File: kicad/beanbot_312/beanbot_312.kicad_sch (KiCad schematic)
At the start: 66 parts, among them M1 P&O2_VOEDING, M10 P&O2_MEETPUNT, M11 P&O2_ULTRASONE_HC_SR04, M12 P&O2_MEETPUNT, M13 P&O2_MEETPUNT, M14 P&O2_GEWICHTSENSOR, M15 P&O2_MEETPUNT, M16 P&O2_MEETPUNT, M17 P&O2_MEETPUNT, M18 P&O2_MEETPUNT, M19 P&O2_MEETPUNT, M2 P&O2_MEETPUNT, M20 P&O2_KLEURSENSOR, M21 P&O2_MEETPUNT, M22 P&O2_MEETPUNT, M23 P&O2_RESISTOR, M24 P&O2_MEETPUNT, M25 P&O2_RESISTOR, M26 P&O2_RESISTOR, M27 P&O2_MEETPUNT, M28 P&O2_DC-MOTOR, M29 P&O2_RESISTOR, M3 P&O2_RESISTOR, M30 P&O2_MEETPUNT, M31 P&O2_DC-MOTOR, M32 P&O2_MEETPUNT, M33 P&O2_RESISTOR, M34 P&O2_MEETPUNT, M35 P&O2_RESISTOR, M36 P&O2_RESISTOR, M37 P&O2_MEETPUNT, M38 P&O2_DC-MOTOR, M39 P&O2_RESISTOR, M4 P&O2_MEETPUNT, M40 P&O2_MEETPUNT, M41 P&O2_DC-MOTOR, M42 P&O2_MEETPUNT, M43 P&O2_RESISTOR, M44 P&O2_MEETPUNT, M45 P&O2_RESISTOR, M46 P&O2_RESISTOR, M47 P&O2_MEETPUNT, M48 P&O2_DC-MOTOR, M49 P&O2_RESISTOR, M5 P&O2_RGB_LED, M50 P&O2_MEETPUNT, M51 P&O2_DC-MOTOR, M52 P&O2_MEETPUNT, M53 P&O2_MOSFET, M54 P&O2_MOSFET, M55 P&O2_MOSFET, M56 P&O2_MOSFET, M57 P&O2_MOSFET, M58 P&O2_MOSFET, M6 P&O2_RESISTOR, M7 P&O2_MEETPUNT, M8 P&O2_RESISTOR, M9 P&O2_RESISTOR, U1 P&O2_ARDUINO_MEGA, U2 LCD-016N002L

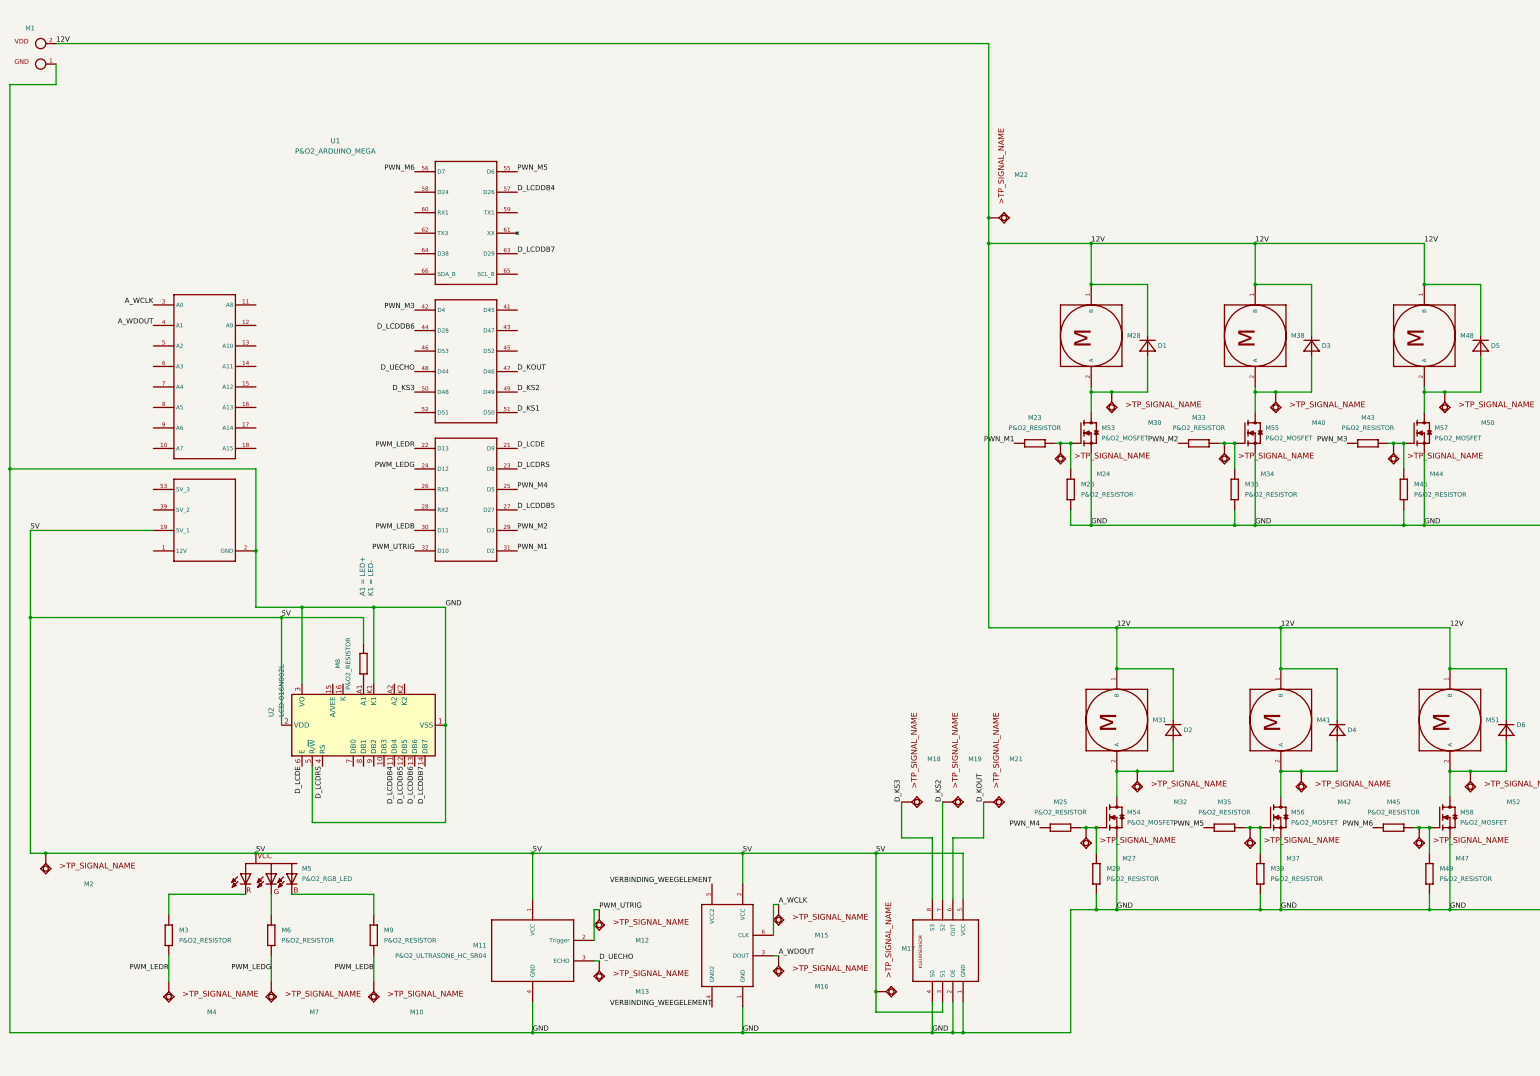
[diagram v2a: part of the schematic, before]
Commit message: Add KiCad changes (#13)
* Added IC to KiCad

* Latest changes

* Fixed scheme

* Changed DC to servomotor

* Latest changes

* Refactored schematic

Co-authored-by: Robin Martens <robin.martens@quivr.be>
Co-authored-by: Rob Nickmans <rob.nickmans@rndevelopment.be>
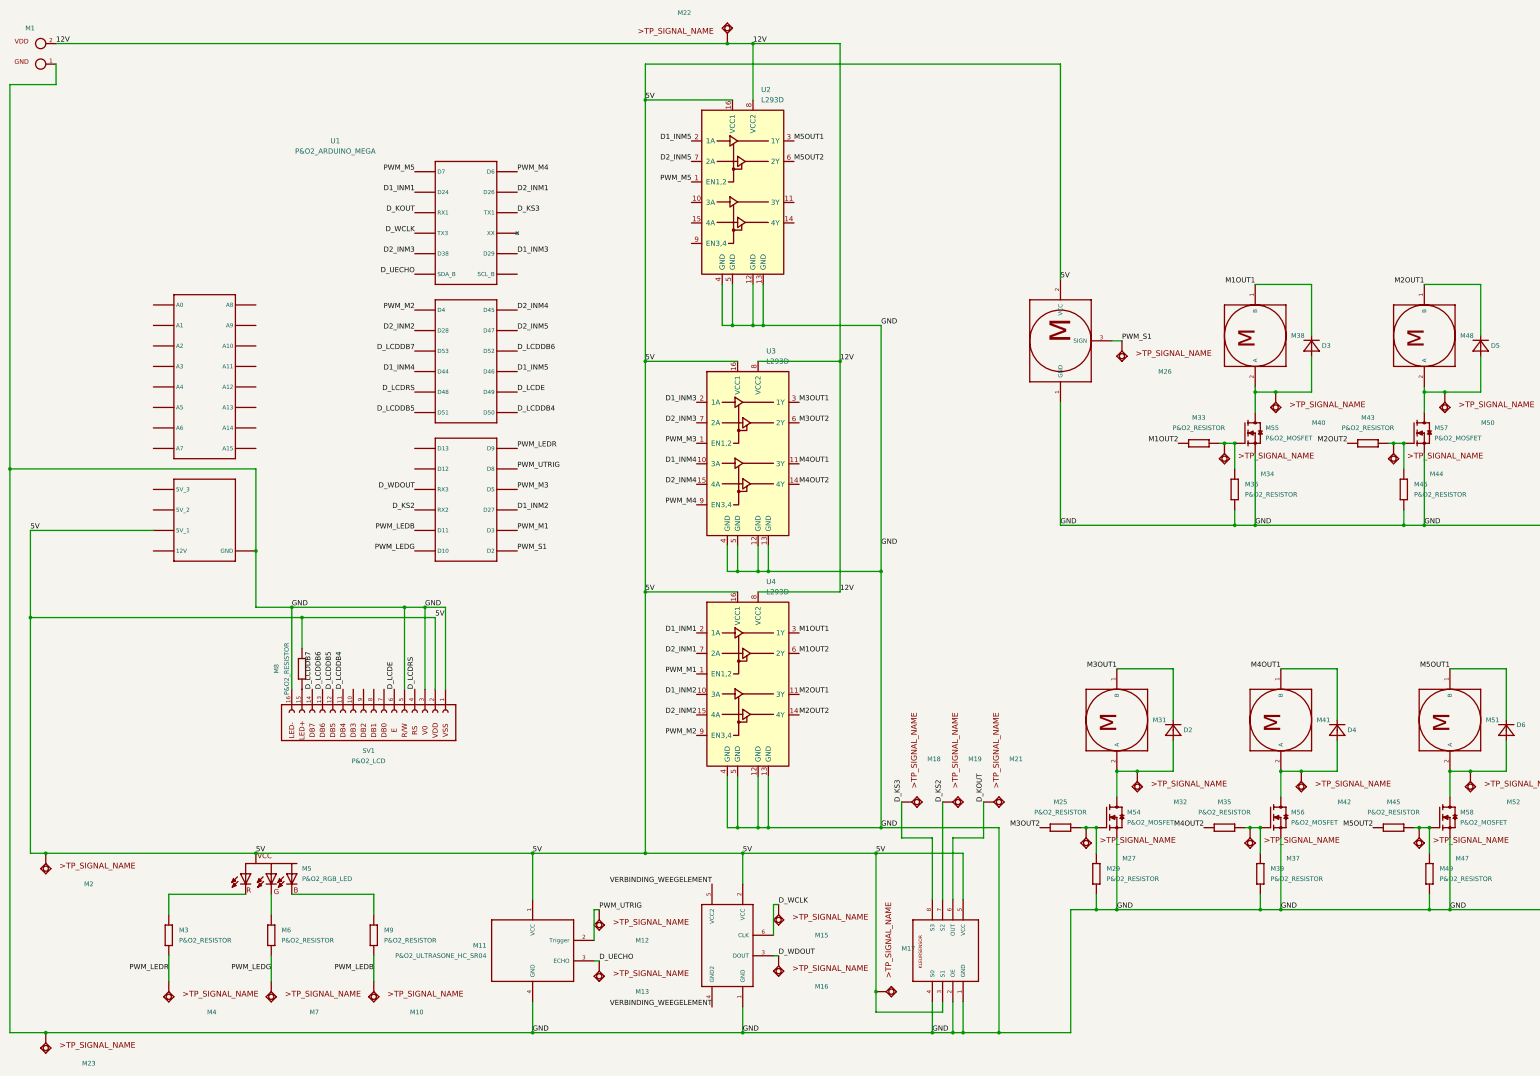
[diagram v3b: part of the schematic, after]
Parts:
- removed D1: P&O2_DIODE, 1_P&O2_lib:P&O2_DIODE, symbol 1_P&O2_lib:P&O2_DIODE
- removed M23, M26: P&O2_RESISTOR, 1_P&O2_lib:P&O2_RES, symbol 1_P&O2_lib:P&O2_RESISTOR
- removed M24, M30: P&O2_MEETPUNT, 1_P&O2_lib:P&O2_MEETPUNT, symbol 1_P&O2_lib:P&O2_MEETPUNT
- removed M28: P&O2_DC-MOTOR, 1_P&O2_lib:P&O2_2PIN-SCREW-5.08, symbol 1_P&O2_lib:P&O2_DC-MOTOR
- removed M53: P&O2_MOSFET, 1_P&O2_lib:P&O2_TO220, symbol 1_P&O2_lib:P&O2_MOSFET
- removed U2: LCD-016N002L, Display:LCD-016N002L, symbol Display_Character:LCD-016N002L
- added M23, M26: P&O2_MEETPUNT, 1_P&O2_lib:P&O2_MEETPUNT, symbol 1_P&O2_lib:P&O2_MEETPUNT
- added M24: P&O2_SERVOMOTOR, P&O2_lib_SERVO-3PIN, symbol 1_P&O2_lib:P&O2_SERVOMOTOR
- added SV1: P&O2_LCD, P&O2_lib_FE05-1, symbol 1_P&O2_lib:P&O2_LCD
- added U2, U3, U4: L293D, Package_DIP:DIP-16_W7.62mm, symbol Driver_Motor:L293D
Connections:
- net D_KS1 is gone; now on net D_LCDDB4: U1.51 (D50)
- net 12V: now also U2.8 (VCC2), U3.8 (VCC2), U4.8 (VCC2); no longer D2.C, D3.C, D4.C, D5.C, D6.C, M31.1 (B), M38.1 (B), M41.1 (B), M48.1 (B), M51.1 (B)
- net 5V: now also M24.2 (VCC), SV1.2, U2.16 (VCC1), U3.16 (VCC1), U4.16 (VCC1)
- net D_KOUT: now also U1.60 (RX1); no longer U1.47 (D46)
- net D_KS2: now also U1.28 (RX2); no longer U1.49 (D49)
- net D_KS3: now also U1.59 (TX1); no longer U1.50 (D48)
- net D_LCDDB4: now also SV1.11; no longer U1.57 (D26)
- net D_LCDDB5: now also U1.52 (D51), SV1.12; no longer U1.27 (D27)
- net D_LCDDB6: now also U1.45 (D52), SV1.13; no longer U1.44 (D28)
- net D_LCDDB7: now also U1.46 (D53), SV1.14; no longer U1.63 (D29)
- net D_LCDE: now also U1.49 (D49), SV1.6; no longer U1.21 (D9)
- net D_LCDRS: now also U1.50 (D48), SV1.4; no longer U1.23 (D8)
- net D_UECHO: now also U1.66 (SDA_B); no longer U1.48 (D44)
- net GND: now also M23.1 (TP), M24.1 (GND), SV1.1, SV1.16, SV1.3, SV1.5, U2.12 (GND), U2.13 (GND), U2.4 (GND), U2.5 (GND), U3.12 (GND), U3.13 (GND), U3.4 (GND), U3.5 (GND), U4.12 (GND), U4.13 (GND), U4.4 (GND), U4.5 (GND)
- net PWM_LEDG: now also U1.32 (D10); no longer U1.24 (D12)
- net PWM_LEDR: now also U1.21 (D9); no longer U1.22 (D13)
- net PWM_UTRIG: now also U1.23 (D8); no longer U1.32 (D10)
- net at M8.1: now also SV1.15
- net D_WDOUT: now reaches U1.26 (RX3)
- net D_WDOUT: now also M14.3 (DOUT), M16.1 (TP)
- net D2_INM4: now reaches U1.41 (D45)
- net D2_INM4: now also U3.15 (4A)
- net D2_INM5: now reaches U1.43 (D47)
- net D2_INM5: now also U2.7 (2A)
- net D1_INM1: now reaches U1.58 (D24)
- net D1_INM1: now also U4.2 (1A)
- net D_WCLK: now reaches U1.62 (TX3)
- net D_WCLK: now also M14.6 (CLK), M15.1 (TP)
- net D2_INM3: now reaches U1.64 (D38)
- net D2_INM3: now also U3.7 (2A)
- removed net A_WCLK: M14.6 (CLK), M15.1 (TP), U1.3 (A0)
- removed net A_WDOUT: M14.3 (DOUT), M16.1 (TP), U1.4 (A1)
- net PWN_M1 renamed PWM_S1
- net PWM_S1: now also M24.3 (SIGN), M26.1 (TP)
- net PWN_M2 renamed M1OUT2
- net M1OUT2: now also U4.6 (2Y); no longer U1.29 (D3)
- net PWN_M3 renamed M2OUT2
- net M2OUT2: now also U4.14 (4Y); no longer U1.42 (D4)
- net PWN_M4 renamed M3OUT2
- net M3OUT2: now also U3.6 (2Y); no longer U1.25 (D5)
- net PWN_M5 renamed M4OUT2
- net M4OUT2: now also U3.14 (4Y); no longer U1.55 (D6)
- net PWN_M6 renamed M5OUT2
- net M5OUT2: now also U2.6 (2Y); no longer U1.56 (D7)
- new net D1_INM2: U1.27 (D27), U4.10 (3A)
- new net D1_INM3: U1.63 (D29), U3.2 (1A)
- new net D1_INM4: U1.48 (D44), U3.10 (3A)
- new net D1_INM5: U1.47 (D46), U2.2 (1A)
- new net D2_INM1: U1.57 (D26), U4.7 (2A)
- new net D2_INM2: U1.44 (D28), U4.15 (4A)
- new net M1OUT1: D3.C, M38.1 (B), U4.3 (1Y)
- new net M2OUT1: D5.C, M48.1 (B), U4.11 (3Y)
- new net M3OUT1: D2.C, M31.1 (B), U3.3 (1Y)
- new net M4OUT1: D4.C, M41.1 (B), U3.11 (3Y)
- new net M5OUT1: D6.C, M51.1 (B), U2.3 (1Y)
- new net PWM_M1: U1.29 (D3), U4.1 (EN1,2)
- new net PWM_M2: U1.42 (D4), U4.9 (EN3,4)
- new net PWM_M3: U1.25 (D5), U3.1 (EN1,2)
- new net PWM_M4: U1.55 (D6), U3.9 (EN3,4)
- new net PWM_M5: U1.56 (D7), U2.1 (EN1,2)
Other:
- note removed: "A1 = LED+ K1 = LED-"
- moved on the sheet: M22

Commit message: Kicad Redraw (#25)
* kicad redraw

* Added labels and measuring point

* Latest KiCad changes

* Restore latest version

Co-authored-by: Robin Martens <robin.martens@quivr.be>
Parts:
- removed D2, D3, D4, D5, D6: P&O2_DIODE, 1_P&O2_lib:P&O2_DIODE, symbol 1_P&O2_lib:P&O2_DIODE
- removed M1: P&O2_VOEDING, 1_P&O2_lib:P&O2_2PIN-SCREW-5.08, symbol 1_P&O2_lib:P&O2_VOEDING
- removed M10, M15, M16, M22, M23, M26, M32, M34, M37, M4, M44, M47, M7: P&O2_MEETPUNT, 1_P&O2_lib:P&O2_MEETPUNT, symbol 1_P&O2_lib:P&O2_MEETPUNT
- removed M14: P&O2_GEWICHTSENSOR, 1_P&O2_lib:P&O2_GEWICHTSENSOR-6PIN, symbol 1_P&O2_lib:P&O2_GEWICHTSENSOR
- removed M24: P&O2_SERVOMOTOR, P&O2_lib_SERVO-3PIN, symbol 1_P&O2_lib:P&O2_SERVOMOTOR
- removed M25, M29, M33, M35, M36, M39, M43, M49: P&O2_RESISTOR, 1_P&O2_lib:P&O2_RES, symbol 1_P&O2_lib:P&O2_RESISTOR
- removed M31, M38, M41, M48, M51: P&O2_DC-MOTOR, 1_P&O2_lib:P&O2_2PIN-SCREW-5.08, symbol 1_P&O2_lib:P&O2_DC-MOTOR
- removed M54, M55, M56, M57, M58: P&O2_MOSFET, 1_P&O2_lib:P&O2_TO220, symbol 1_P&O2_lib:P&O2_MOSFET
- removed U1: P&O2_ARDUINO_MEGA, 1_P&O2_lib:P&O2_ARDUINO_MEGA, symbol 1_P&O2_lib:P&O2_ARDUINO_MEGA
- removed U2, U3, U4: L293D, Package_DIP:DIP-16_W7.62mm, symbol Driver_Motor:L293D
- added M12, M19, M2, M20, M28, M38, M39, M41, M43, M51, M6: P&O2_MEETPUNT, 1_P&O2_lib:P&O2_MEETPUNT, symbol 1_P&O2_lib:P&O2_MEETPUNT
- added M13, M3, M7: P&O2_RESISTOR, 1_P&O2_lib:P&O2_RES, symbol 1_P&O2_lib:P&O2_RESISTOR
- added M14, M4, M47, M48, M49, M8: P&O2_MOSFET, 1_P&O2_lib:P&O2_TO220, symbol 1_P&O2_lib:P&O2_MOSFET
- added M21: P&O2_GEWICHTSENSOR2, 1_P&O2_lib:P&O2_GEWICHTSENSOR-4PIN, symbol 1_P&O2_lib:P&O2_GEWICHTSENSOR2
- added M29, M31, M33: P&O2_RELAIS-DP, 1_P&O2_lib:P&O2_RELAY-DP, symbol 1_P&O2_lib:P&O2_RELAIS-DP
- added M30, M32, M34: P&O2_DC-MOTOR, 1_P&O2_lib:P&O2_2PIN-SCREW-5.08, symbol 1_P&O2_lib:P&O2_DC-MOTOR
- added M35, M36, M37: P&O2_DIODE, 1_P&O2_lib:P&O2_DIODE, symbol 1_P&O2_lib:P&O2_DIODE
- added M44: P&O2_RESISTOR, 1_P&O2_lib:P&O2_RESISTOR, symbol 1_P&O2_lib:P&O2_RESISTOR
- added U1: P&O2_ARDUINO_MEGA_SHIELD, 1_P&O2_lib:P&O2_ARDUINO_MEGA_SHIELD, symbol 1_P&O2_lib:P&O2_ARDUINO_MEGA_SHIELD
- M45, M46: footprint 1_P&O2_lib:P&O2_RES -> 1_P&O2_lib:P&O2_RESISTOR
- SV1: footprint P&O2_lib_FE05-1 -> (none)
- renumbered M2 to M1, M5 to M10, M8 to M11, M9 to M15, M11 to M16, M12 to M17, M13 to M18, M17 to M22, M18 to M23, M19 to M24, M20 to M25, M21 to M26, M3 to M5, M6 to M9
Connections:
- net M5OUT2 is gone; now on net PWM_M2: M45.1
- net 12V: now also M28.1 (TP), M29.12 (1), M29.24 (1), M31.12 (1), M31.24 (1), M33.12 (1), M33.24 (1), M35.C, M36.C, M37.C, U1.1 (12V)
- net 5V: now also M21.1 (VCC), U1.19 (5V_1)
- net D_KOUT: now also U1.60 (RX1)
- net D_KS2: now also U1.28 (RX2)
- net D_KS3: now also U1.59 (TX1)
- net D_LCDDB4: now also U1.51 (D50)
- net D_LCDDB5: now also U1.52 (D51)
- net D_LCDDB6: now also U1.45 (D52)
- net D_LCDDB7: now also U1.46 (D53)
- net D_LCDE: now also U1.49 (D49)
- net D_LCDRS: now also U1.50 (D48)
- net D_UECHO: now also U1.62 (TX3)
- net GND: now also M27.1 (TP), M40.1 (TP), M45.2, M13.2, M14.3 (S), M21.2 (GND), M29.14 (1), M29.22 (1), M29.A2 (2), M3.2, M31.14 (1), M31.22 (1), M31.A2 (2), M33.14 (1), M33.22 (1), M33.A2 (2), M35.A, M36.A, M37.A, M38.1 (TP), M39.1 (TP), M4.3 (S), M44.2, M47.2 (D), M47.3 (S), M48.2 (D), M48.3 (S), M49.2 (D), M49.3 (S), M7.2, M8.3 (S)
- net PWM_LEDB: now also M12.1 (TP), M13.1, M14.1 (eG), U1.30 (D11); no longer M15.2
- net PWM_LEDG: now also M6.1 (TP), M7.1, M8.1 (eG), U1.32 (D10); no longer M9.2
- net PWM_LEDR: now also M2.1 (TP), M3.1, M4.1 (eG), U1.21 (D9); no longer M5.2
- net PWM_M1: now also M46.1, M43.1 (TP), M49.1 (eG), U1.31 (D2)
- net PWM_M2: now also M42.1 (TP), M48.1 (eG), U1.29 (D3)
- net PWM_M3: now also M41.1 (TP), M44.1, M47.1 (eG), U1.42 (D4)
- net PWM_UTRIG: now also U1.23 (D8)
- net D_RELM1: now reaches M52.1 (TP)
- net D_RELM1: now also M33.A1 (1), U1.58 (D24)
- net D_RELM3: now reaches M50.1 (TP)
- net D_RELM3: now also M29.A1 (1), U1.27 (D27)
- new net: M33.11 (1), M34.1 (B)
- new net: M33.21 (1), M34.2 (A)
- new net: M29.11 (1), M30.1 (B)
- new net: M29.21 (1), M30.2 (A)
- new net: M31.11 (1), M32.1 (B)
- new net: M31.21 (1), M32.2 (A)
- new net: M8.2 (D), M9.2
- new net: M4.2 (D), M5.2
- new net: M14.2 (D), M15.2
- new net D_RELM2: M31.A1 (1), M51.1 (TP), U1.57 (D26)
- new net D_WSCL: M19.1 (TP), M21.3 (SCL), U1.65 (SCL_B)
- new net D_WSDA: M20.1 (TP), M21.4 (SDA), U1.66 (SDA_B)
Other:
- moved on the sheet: M5, M9

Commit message: PCB (#28)
* Made outline for pcb

* Moved all components for an overview

* First attempt for DC motor & tweaked scheme a little

* Almost finished

* Fix warnings

* Add forgotten file

* Deleted hidden 5V label

* Added footprints

* Updated pcb

* Some progress on the PCB

* Latest changes

* Change border

* Finished PCB

* Changed team name location

* Final changes to PCB

* Cleared warnings

Co-authored-by: Robin Martens <robin.martens@quivr.be>
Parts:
- removed M22, M40, M43, M52: P&O2_MEETPUNT, 1_P&O2_lib:P&O2_MEETPUNT, symbol 1_P&O2_lib:P&O2_MEETPUNT
- removed M33: P&O2_RELAIS-DP, 1_P&O2_lib:P&O2_RELAY-DP, symbol 1_P&O2_lib:P&O2_RELAIS-DP
- removed M34: P&O2_DC-MOTOR, 1_P&O2_lib:P&O2_2PIN-SCREW-5.08, symbol 1_P&O2_lib:P&O2_DC-MOTOR
- removed M37: P&O2_DIODE, 1_P&O2_lib:P&O2_DIODE, symbol 1_P&O2_lib:P&O2_DIODE
- removed M46: P&O2_RESISTOR, 1_P&O2_lib:P&O2_RESISTOR, symbol 1_P&O2_lib:P&O2_RESISTOR
- removed M49: P&O2_MOSFET, 1_P&O2_lib:P&O2_TO220, symbol 1_P&O2_lib:P&O2_MOSFET
- M11, M13, M15, M3, M5, M7, M9: footprint 1_P&O2_lib:P&O2_RES -> 1_P&O2_lib:P&O2_RESISTOR
- SV1: footprint (none) -> 1_P&O2_lib:P&O2_LCD
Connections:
- net D_RELM1 is gone; now on net D_RELM2: U1.58 (D24)
- net D_KOUT: now also U1.64 (D38); no longer U1.60 (RX1)
- net D_KS2: now also U1.62 (TX3); no longer U1.28 (RX2)
- net D_KS3: now also U1.60 (RX1); no longer U1.59 (TX1)
- net D_LCDDB4: now also U1.47 (D46); no longer U1.51 (D50)
- net D_LCDDB5: now also U1.45 (D52); no longer U1.52 (D51)
- net D_LCDDB6: now also U1.43 (D47); no longer U1.45 (D52)
- net D_LCDDB7: now also U1.41 (D45); no longer U1.46 (D53)
- net D_LCDRS: now also U1.51 (D50); no longer U1.50 (D48)
- net D_RELM2: no longer U1.57 (D26)
- net D_RELM3: now also U1.57 (D26); no longer U1.27 (D27)
- net D_UECHO: now also U1.28 (RX2); no longer U1.62 (TX3)
- net GND: no longer M29.14 (1), M29.22 (1), M31.14 (1), M31.22 (1), M35.A, M36.A, M38.1 (TP), M39.1 (TP), M47.2 (D), M48.2 (D)
- net PWM_LEDB: now also U1.22 (D13); no longer U1.30 (D11)
- net PWM_LEDG: now also U1.24 (D12); no longer U1.32 (D10)
- net PWM_LEDR: now also U1.30 (D11); no longer U1.21 (D9)
- net PWM_M2: now also U1.56 (D7); no longer U1.29 (D3)
- net PWM_M3: now also U1.55 (D6); no longer U1.42 (D4)
- net PWM_UTRIG: now also U1.32 (D10); no longer U1.23 (D8)
- net PWM_M1: no longer names the net of U1.31 (D2)
- new net: M29.14 (1), M29.22 (1), M35.A, M38.1 (TP), M47.2 (D)
- new net: M31.14 (1), M31.22 (1), M36.A, M39.1 (TP), M48.2 (D)

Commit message: Backups
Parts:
- added M37, M40: P&O2_RESISTOR, 1_P&O2_lib:P&O2_RESISTOR, symbol 1_P&O2_lib:P&O2_RESISTOR
- added M43, M46: P&O2_MOSFET, 1_P&O2_lib:P&O2_TO220, symbol 1_P&O2_lib:P&O2_MOSFET
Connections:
- net D_RELM2: now also M40.1, M46.1 (eG); no longer M31.A1 (1)
- net D_RELM3: now also M37.1, M43.1 (eG); no longer M29.A1 (1)
- net GND: now also M37.2, M40.2, M43.3 (S), M46.3 (S)
- new net: M31.A1 (1), M46.2 (D)
- new net: M29.A1 (1), M43.2 (D)
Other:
- moved on the sheet: M32, M36, M39, M42, M45, M48, M50, M51

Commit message: Edited kicad scheme and pcb
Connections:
- net 5V: now also M29.A2 (2), M31.A2 (2)
- net GND: no longer M29.A2 (2), M31.A2 (2)

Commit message: Changes
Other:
- company: (none) -> KU Leuven
- title: (none) -> Elektrisch schema team 312
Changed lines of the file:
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@@
 (kicad_sch (version 20211123) (generator eeschema)
   (paper "A3")
+  (title_block
+    (title "Elektrisch schema team 312")
+    (date "2022-05-18")
+    (company "KU Leuven")
+  )
   (junction (at 63.5 256.54) (diameter 0) (color 0 0 0 0)
   )
@@
     (effects (font (size 1.27 1.27)) (justify left bottom))
   )
+  (label "5V" (at 359.41 205.74 0)
+    (effects (font (size 1.27 1.27)) (justify left bottom))
+  )
   (label "D_KS3" (at 116.84 64.77 180)
     (effects (font (size 1.27 1.27)) (justify right bottom))
@@
     (effects (font (size 1.27 1.27)) (justify left bottom))
   )
+  (label "GND" (at 337.82 240.03 0)
+    (effects (font (size 1.27 1.27)) (justify left bottom))
+  )
   (label "D_LCDE" (at 142.24 109.22 0)
     (effects (font (size 1.27 1.27)) (justify left bottom))
@@
     (effects (font (size 1.27 1.27)) (justify left bottom))
   )
+  (label "GND" (at 359.41 240.03 0)
+    (effects (font (size 1.27 1.27)) (justify left bottom))
+  )
   (label "12V" (at 304.8 54.61 180)
     (effects (font (size 1.27 1.27)) (justify right bottom))
   )
+  (label "GND" (at 358.14 127 0)
+    (effects (font (size 1.27 1.27)) (justify left bottom))
+  )
   (label "D_LCDDB6" (at 93.98 182.88 90)
     (effects (font (size 1.27 1.27)) (justify left bottom))
@@
     (effects (font (size 1.27 1.27)) (justify right bottom))
   )
+  (label "5V" (at 358.14 92.71 0)
+    (effects (font (size 1.27 1.27)) (justify left bottom))
+  )
   (label "D_LCDE" (at 111.76 182.88 90)
     (effects (font (size 1.27 1.27)) (justify left bottom))
@@
     (effects (font (size 1.27 1.27)) (justify left bottom))
   )
+  (label "GND" (at 353.06 127 0)
+    (effects (font (size 1.27 1.27)) (justify left bottom))
+  )
